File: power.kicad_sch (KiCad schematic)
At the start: 63 parts, among them Q1 AO3401A, Q2 AO3401A, Q21 FS8205A, Q6 2N7002, U10 BQ27546, U27 TPS63001, U29 BQ24081, U30 DW01+G, U6 TPS61040DBV

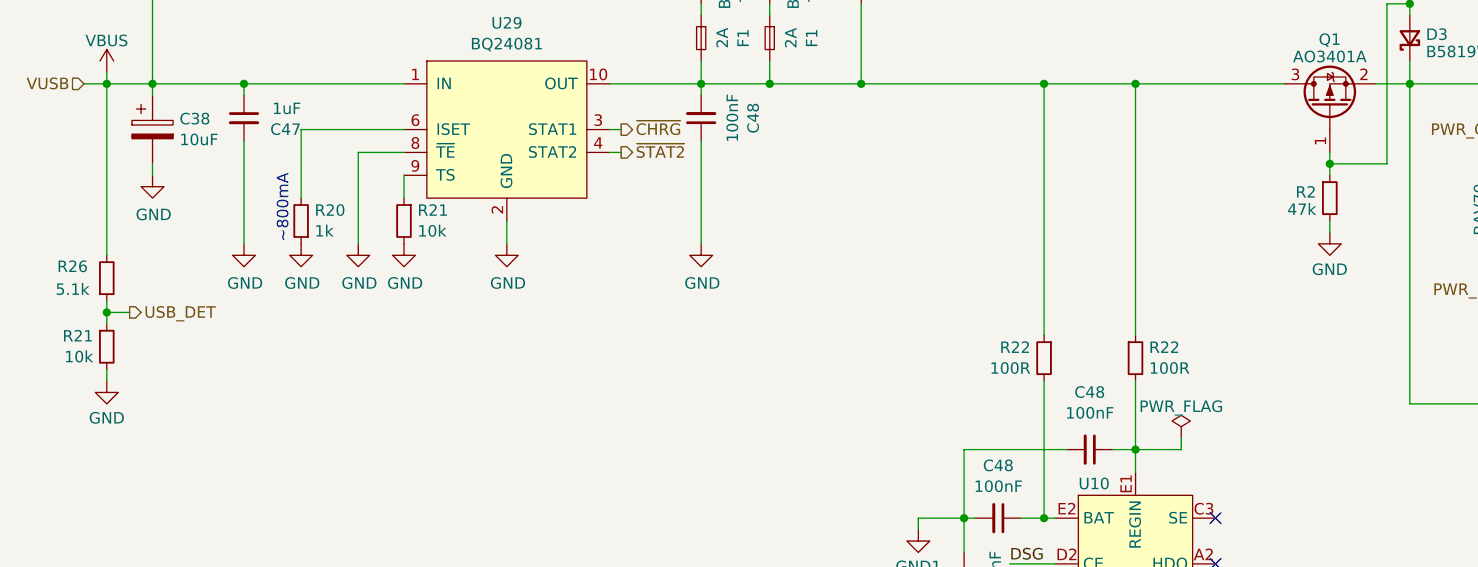
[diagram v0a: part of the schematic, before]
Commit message: Start rev1.1
Fixed bugs:
 - Swapped D+ and D-
 - Insufficient pull-down strength on VBUS
 - Default OLED to 4-wire SPI
 - Swap VBUS detect divider from 2/3 to 1/3
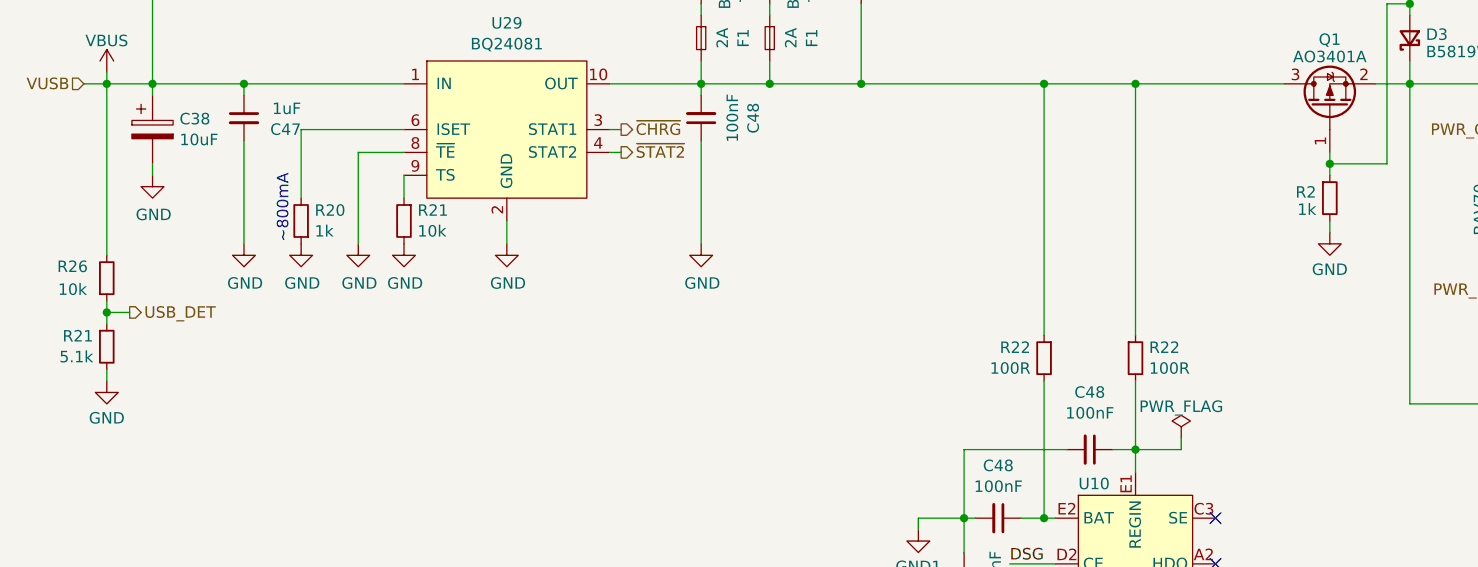
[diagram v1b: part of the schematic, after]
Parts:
- R2: value 47k -> 1k; LCSC C25792 -> C11702
- R21: value 10k -> 5.1k; LCSC C25744 -> C25905
- R26: value 5.1k -> 10k; LCSC C25905 -> C25744
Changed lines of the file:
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@@
       (effects (font (size 1.27 1.27)) (justify right))
     )
-    (property "Value" "10k" (at 21.3614 77.343 0)
+    (property "Value" "5.1k" (at 21.3614 77.343 0)
       (effects (font (size 1.27 1.27)) (justify right))
     )
@@
       (effects (font (size 1.27 1.27)) hide)
     )
-    (property "LCSC" "C25744" (at 22.86 76.2 0)
+    (property "LCSC" "C25905" (at 22.86 76.2 0)
       (effects (font (size 1.27 1.27)) hide)
     )
@@
       (effects (font (size 1.27 1.27)) (justify right))
     )
-    (property "Value" "47k" (at 157.2514 60.9673 0)
+    (property "Value" "1k" (at 157.2514 60.9673 0)
       (effects (font (size 1.27 1.27)) (justify right))
     )
@@
       (effects (font (size 1.27 1.27)) hide)
     )
-    (property "LCSC" "C25792" (at 158.75 59.69 0)
+    (property "LCSC" "C11702" (at 158.75 59.69 0)
       (effects (font (size 1.27 1.27)) hide)
     )
@@
       (effects (font (size 1.27 1.27)))
     )
-    (property "Value" "5.1k" (at 19.05 69.85 0)
+    (property "Value" "10k" (at 19.05 69.85 0)
       (effects (font (size 1.27 1.27)))
     )
@@
       (effects (font (size 1.27 1.27)) hide)
     )
-    (property "LCSC" "C25905" (at 22.86 68.58 0)
-      (effects (font (size 1.27 1.27)) hide)
-    )
+    (property "LCSC" "C25744" (at 22.86 68.58 0)
+      (effects (font (size 1.27 1.27)) hide)
+    )

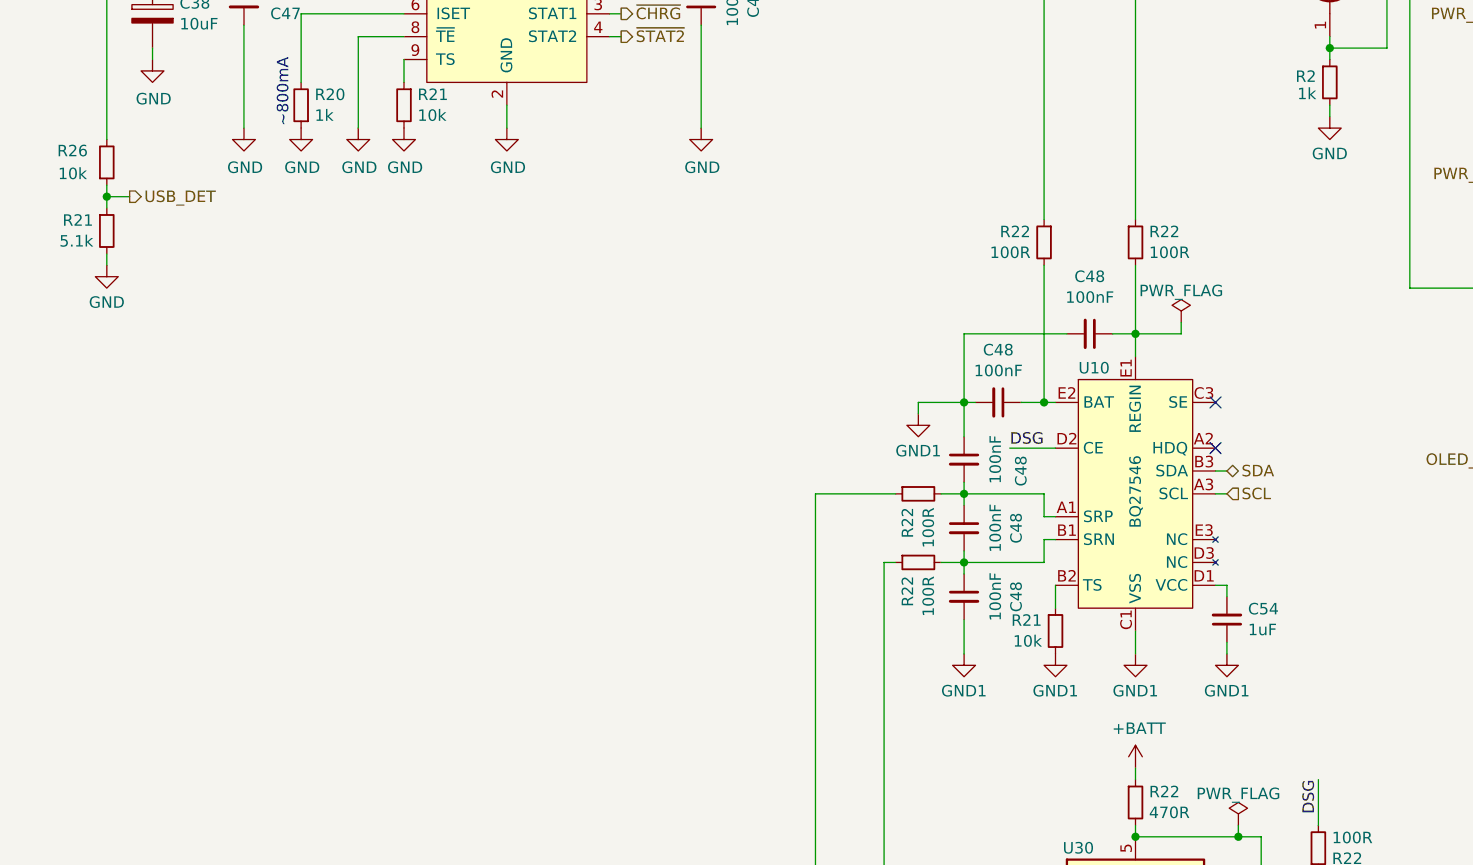
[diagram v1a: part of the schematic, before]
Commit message: More Rev 1.1 fixes
- Revert USB_DET voltage divider swap
- Fix battery gauge temperature sensor reference level
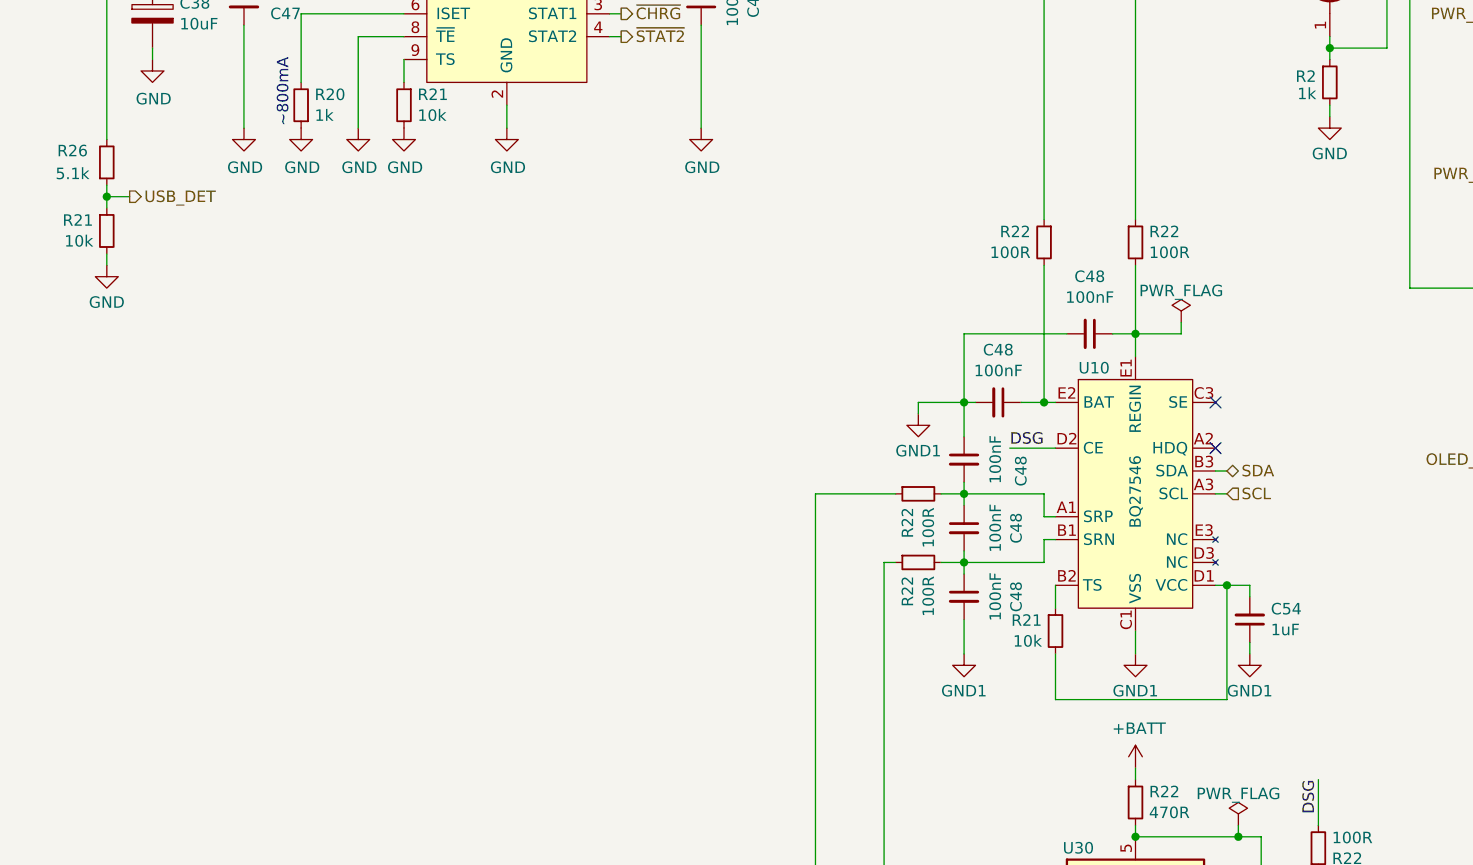
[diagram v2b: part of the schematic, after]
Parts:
- R21: value 5.1k -> 10k; LCSC C25905 -> C25744
- R26: value 10k -> 5.1k; LCSC C25744 -> C25905
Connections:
- net GND1: no longer R21.2
- net at C54.2, U10.D1 (VCC): now also R21.2
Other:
- moved on the sheet: C54
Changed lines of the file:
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@@
   (junction (at 205.74 46.99) (diameter 0) (color 0 0 0 0)
   )
+  (junction (at 147.32 115.57) (diameter 0) (color 0 0 0 0)
+  )
   (junction (at 231.14 93.98) (diameter 0) (color 0 0 0 0)
   )
@@
     (stroke (width 0) (type default))
   )
+  (wire (pts (xy 128.27 128.27) (xy 147.32 128.27))
+    (stroke (width 0) (type default))
+  )
   (wire (pts (xy 195.58 46.99) (xy 195.58 48.26))
     (stroke (width 0) (type default))
@@
     (stroke (width 0) (type default))
   )
+  (wire (pts (xy 147.32 128.27) (xy 147.32 115.57))
+    (stroke (width 0) (type default))
+  )
   (wire (pts (xy 127 46.99) (xy 127 74.93))
     (stroke (width 0) (type default))
@@
     (stroke (width 0) (type default))
   )
-  (wire (pts (xy 147.32 123.19) (xy 147.32 121.92))
+  (wire (pts (xy 149.86 123.19) (xy 149.86 121.92))
     (stroke (width 0) (type default))
   )
@@
     (stroke (width 0) (type default))
   )
+  (wire (pts (xy 147.32 115.57) (xy 149.86 115.57))
+    (stroke (width 0) (type default))
+  )
   (wire (pts (xy 186.69 91.44) (xy 186.69 82.55))
     (stroke (width 0) (type default))
@@
     (stroke (width 0) (type default))
   )
+  (wire (pts (xy 128.27 123.19) (xy 128.27 128.27))
+    (stroke (width 0) (type default))
+  )
   (wire (pts (xy 243.84 101.6) (xy 237.49 101.6))
     (stroke (width 0) (type default))
@@
     (stroke (width 0) (type default))
   )
-  (wire (pts (xy 147.32 115.57) (xy 147.32 116.84))
+  (wire (pts (xy 149.86 115.57) (xy 149.86 116.84))
     (stroke (width 0) (type default))
   )
@@
     )
   )
-  (symbol (lib_id "power:GND1") (at 128.27 123.19 0) (unit 1)
-    (in_bom yes) (on_board yes) (dnp no) (fields_autoplaced)
-    (property "Reference" "#PWR035" (at 128.27 129.54 0)
-      (effects (font (size 1.27 1.27)) hide)
-    )
-    (property "Value" "GND1" (at 128.27 127.3255 0)
-      (effects (font (size 1.27 1.27)))
-    )
-    (property "Footprint" "" (at 128.27 123.19 0)
-      (effects (font (size 1.27 1.27)) hide)
-    )
-    (property "Datasheet" "" (at 128.27 123.19 0)
-      (effects (font (size 1.27 1.27)) hide)
-    )
-    (pin "1")
-    (instances
-      (project "oled-nametag"
-        (path "/c0b8a503-1da4-4e1a-941c-dddf39a5c519/b1f1b085-615b-4d75-b80e-4b089a5e74f7"
-          (reference "#PWR035") (unit 1)
-        )
-      )
-    )
-  )
   (symbol (lib_id "power:VBUS") (at 22.86 45.72 0) (unit 1)
     (in_bom yes) (on_board yes) (dnp no) (fields_autoplaced)
@@
       (effects (font (size 1.27 1.27)) (justify right))
     )
-    (property "Value" "5.1k" (at 21.3614 77.343 0)
+    (property "Value" "10k" (at 21.3614 77.343 0)
       (effects (font (size 1.27 1.27)) (justify right))
     )
@@
       (effects (font (size 1.27 1.27)) hide)
     )
-    (property "LCSC" "C25905" (at 22.86 76.2 0)
+    (property "LCSC" "C25744" (at 22.86 76.2 0)
       (effects (font (size 1.27 1.27)) hide)
     )
@@
     )
   )
-  (symbol (lib_id "Device:C_Small") (at 147.32 119.38 180) (unit 1)
+  (symbol (lib_id "Device:C_Small") (at 149.86 119.38 180) (unit 1)
     (in_bom yes) (on_board yes) (dnp no)
-    (property "Reference" "C54" (at 149.6568 118.2116 0)
+    (property "Reference" "C54" (at 152.1968 118.2116 0)
       (effects (font (size 1.27 1.27)) (justify right))
     )
-    (property "Value" "1uF" (at 149.6568 120.523 0)
+    (property "Value" "1uF" (at 152.1968 120.523 0)
       (effects (font (size 1.27 1.27)) (justify right))
     )
-    (property "Footprint" "Capacitor_SMD:C_0402_1005Metric" (at 147.32 119.38 0)
+    (property "Footprint" "Capacitor_SMD:C_0402_1005Metric" (at 149.86 119.38 0)
       (effects (font (size 1.27 1.27)) hide)
     )
-    (property "Datasheet" "~" (at 147.32 119.38 0)
+    (property "Datasheet" "~" (at 149.86 119.38 0)
       (effects (font (size 1.27 1.27)) hide)
     )
-    (property "LCSC" "C52923" (at 147.32 119.38 0)
+    (property "LCSC" "C52923" (at 149.86 119.38 0)
       (effects (font (size 1.27 1.27)) hide)
     )
@@
       (effects (font (size 1.27 1.27)))
     )
-    (property "Value" "10k" (at 19.05 69.85 0)
+    (property "Value" "5.1k" (at 19.05 69.85 0)
       (effects (font (size 1.27 1.27)))
     )
@@
       (effects (font (size 1.27 1.27)) hide)
     )
-    (property "LCSC" "C25744" (at 22.86 68.58 0)
+    (property "LCSC" "C25905" (at 22.86 68.58 0)
       (effects (font (size 1.27 1.27)) hide)
     )
@@
     )
   )
-  (symbol (lib_id "power:GND1") (at 147.32 123.19 0) (unit 1)
+  (symbol (lib_id "power:GND1") (at 149.86 123.19 0) (unit 1)
     (in_bom yes) (on_board yes) (dnp no) (fields_autoplaced)
-    (property "Reference" "#PWR042" (at 147.32 129.54 0)
+    (property "Reference" "#PWR042" (at 149.86 129.54 0)
       (effects (font (size 1.27 1.27)) hide)
     )
-    (property "Value" "GND1" (at 147.32 127.3255 0)
+    (property "Value" "GND1" (at 149.86 127.3255 0)
       (effects (font (size 1.27 1.27)))
     )
-    (property "Footprint" "" (at 147.32 123.19 0)
+    (property "Footprint" "" (at 149.86 123.19 0)
       (effects (font (size 1.27 1.27)) hide)
     )
-    (property "Datasheet" "" (at 147.32 123.19 0)
+    (property "Datasheet" "" (at 149.86 123.19 0)
       (effects (font (size 1.27 1.27)) hide)
     )

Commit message: Reduce charge current to 300mA, Add battery voltage calibration testpoint
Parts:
- added TP10: VCAL, TestPoint:TestPoint_Pad_1.0x1.0mm, symbol Connector:TestPoint
- R20: value 1k -> 2.7k; footprint Resistor_SMD:R_0402_1005Metric -> Resistor_SMD:R_0603_1608Metric; LCSC C11702 -> C13167
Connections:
- net at C48.1, R22.2, U10.E2 (BAT): now also TP10.1
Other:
- note added: "~300mA"
- note removed: "~800mA"
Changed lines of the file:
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@@
   (junction (at 167.64 46.99) (diameter 0) (color 0 0 0 0)
   )
+  (junction (at 127 82.55) (diameter 0) (color 0 0 0 0)
+  )
   (junction (at 210.82 46.99) (diameter 0) (color 0 0 0 0)
   )
@@
     (stroke (width 0) (type default))
   )
+  (wire (pts (xy 127 82.55) (xy 127 95.25))
+    (stroke (width 0) (type default))
+  )
   (wire (pts (xy 185.42 60.96) (xy 186.69 60.96))
     (stroke (width 0) (type default))
@@
     (stroke (width 0) (type default))
   )
+  (wire (pts (xy 111.76 82.55) (xy 127 82.55))
+    (stroke (width 0) (type default))
+  )
   (wire (pts (xy 237.49 60.96) (xy 257.81 60.96))
     (stroke (width 0) (type default))
@@
     (stroke (width 0) (type default))
   )
+  (wire (pts (xy 111.76 80.01) (xy 111.76 82.55))
+    (stroke (width 0) (type default))
+  )
   (wire (pts (xy 137.16 135.89) (xy 137.16 137.16))
     (stroke (width 0) (type default))
@@
     (stroke (width 0) (type default))
   )
-  (wire (pts (xy 127 80.01) (xy 127 95.25))
+  (wire (pts (xy 127 80.01) (xy 127 82.55))
     (stroke (width 0) (type default))
   )
@@
     (stroke (width 0) (type default))
   )
-  (text "~800mA" (at 43.18 64.77 90)
+  (text "~300mA" (at 43.18 64.77 90)
     (effects (font (size 1.27 1.27)) (justify left bottom))
   )
@@
       (effects (font (size 1.27 1.27)) (justify right))
     )
-    (property "Value" "1k" (at 45.9486 63.373 0)
+    (property "Value" "2.7k" (at 45.9486 63.373 0)
       (effects (font (size 1.27 1.27)) (justify right))
     )
-    (property "Footprint" "Resistor_SMD:R_0402_1005Metric" (at 44.45 62.23 0)
+    (property "Footprint" "Resistor_SMD:R_0603_1608Metric" (at 44.45 62.23 0)
       (effects (font (size 1.27 1.27)) hide)
     )
@@
       (effects (font (size 1.27 1.27)) hide)
     )
-    (property "LCSC" "C11702" (at 44.45 62.23 0)
+    (property "LCSC" "C13167" (at 44.45 62.23 0)
       (effects (font (size 1.27 1.27)) hide)
     )
@@
         )
       )
+    )
+  )
+  (symbol (lib_id "Connector:TestPoint") (at 111.76 80.01 0) (unit 1)
+    (in_bom no) (on_board yes) (dnp no) (fields_autoplaced)
+    (property "Reference" "TP10" (at 113.157 76.0643 0)
+      (effects (font (size 1.27 1.27)) (justify left))
+    )
+    (property "Value" "VCAL" (at 113.157 77.9853 0)
+      (effects (font (size 1.27 1.27)) (justify left))
+    )
+    (property "Footprint" "TestPoint:TestPoint_Pad_1.0x1.0mm" (at 116.84 80.01 0)
+      (effects (font (size 1.27 1.27)) hide)
+    )
+    (property "Datasheet" "~" (at 116.84 80.01 0)
+      (effects (font (size 1.27 1.27)) hide)
+    )
+    (pin "1")
+    (instances
+      (project "oled-nametag"
+        (path "/c0b8a503-1da4-4e1a-941c-dddf39a5c519/b1f1b085-615b-4d75-b80e-4b089a5e74f7"
+          (reference "TP10") (unit 1)
+        )
+      )

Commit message: Add current calibration output
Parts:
- added J3: LOAD, Connector_PinHeader_2.54mm:PinHeader_1x02_P2.54mm_Vertical, symbol Connector_Generic:Conn_01x02
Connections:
- net +BATT: now also J3.1 (Pin_1)
- net GND: now also J3.2 (Pin_2)
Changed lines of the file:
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@@
+    (stroke (width 0) (type default))
+  )
+  (wire (pts (xy 142.24 39.37) (xy 140.97 39.37))
+    (stroke (width 0) (type default))
+  )
+  (wire (pts (xy 142.24 39.37) (xy 142.24 40.64))
     (stroke (width 0) (type default))
   )
@@
     (stroke (width 0) (type default))
   )
+  (wire (pts (xy 137.16 39.37) (xy 138.43 39.37))
+    (stroke (width 0) (type default))
+  )
   (wire (pts (xy 194.31 91.44) (xy 194.31 90.17))
     (stroke (width 0) (type default))
@@
     (stroke (width 0) (type default))
   )
+  (wire (pts (xy 138.43 39.37) (xy 138.43 38.1))
+    (stroke (width 0) (type default))
+  )
   (wire (pts (xy 195.58 46.99) (xy 205.74 46.99))
     (stroke (width 0) (type default))
@@
     (stroke (width 0) (type default))
   )
+  (wire (pts (xy 137.16 46.99) (xy 137.16 39.37))
+    (stroke (width 0) (type default))
+  )
   (wire (pts (xy 229.87 33.02) (xy 237.49 33.02))
     (stroke (width 0) (type default))
@@
   )
   (wire (pts (xy 237.49 60.96) (xy 257.81 60.96))
+    (stroke (width 0) (type default))
+  )
+  (wire (pts (xy 140.97 38.1) (xy 140.97 39.37))
     (stroke (width 0) (type default))
   )
@@
     )
   )
+  (symbol (lib_id "Connector_Generic:Conn_01x02") (at 138.43 33.02 90) (unit 1)
+    (in_bom yes) (on_board yes) (dnp no) (fields_autoplaced)
+    (property "Reference" "J3" (at 143.002 31.996 90)
+      (effects (font (size 1.27 1.27)) (justify right))
+    )
+    (property "Value" "LOAD" (at 143.002 34.044 90)
+      (effects (font (size 1.27 1.27)) (justify right))
+    )
+    (property "Footprint" "Connector_PinHeader_2.54mm:PinHeader_1x02_P2.54mm_Vertical" (at 138.43 33.02 0)
+      (effects (font (size 1.27 1.27)) hide)
+    )
+    (property "Datasheet" "~" (at 138.43 33.02 0)
+      (effects (font (size 1.27 1.27)) hide)
+    )
+    (pin "1")
+    (pin "2")
+    (instances
+      (project "oled-nametag"
+        (path "/c0b8a503-1da4-4e1a-941c-dddf39a5c519/b1f1b085-615b-4d75-b80e-4b089a5e74f7"
+          (reference "J3") (unit 1)
+        )
+      )
+    )
+  )
   (symbol (lib_id "power:GND") (at 38.1 64.77 0) (unit 1)
     (in_bom yes) (on_board yes) (dnp no)
@@
         )
       )
+    )
+  )
+  (symbol (lib_id "power:GND") (at 142.24 40.64 0) (unit 1)
+    (in_bom yes) (on_board yes) (dnp no) (fields_autoplaced)
+    (property "Reference" "#PWR03" (at 142.24 46.99 0)
+      (effects (font (size 1.27 1.27)) hide)
+    )
+    (property "Value" "GND" (at 142.24 44.585 0)
+      (effects (font (size 1.27 1.27)))
+    )
+    (property "Footprint" "" (at 142.24 40.64 0)
+      (effects (font (size 1.27 1.27)) hide)
+    )
+    (property "Datasheet" "" (at 142.24 40.64 0)
+      (effects (font (size 1.27 1.27)) hide)
+    )
+    (pin "1")
+    (instances
+      (project "oled-nametag"
+        (path "/c0b8a503-1da4-4e1a-941c-dddf39a5c519/b1f1b085-615b-4d75-b80e-4b089a5e74f7"
+          (reference "#PWR03") (unit 1)
+        )
+      )
